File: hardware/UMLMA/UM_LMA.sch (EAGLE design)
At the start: 10 parts, among them IC1 TINY13, J1 AVRISP6_TP

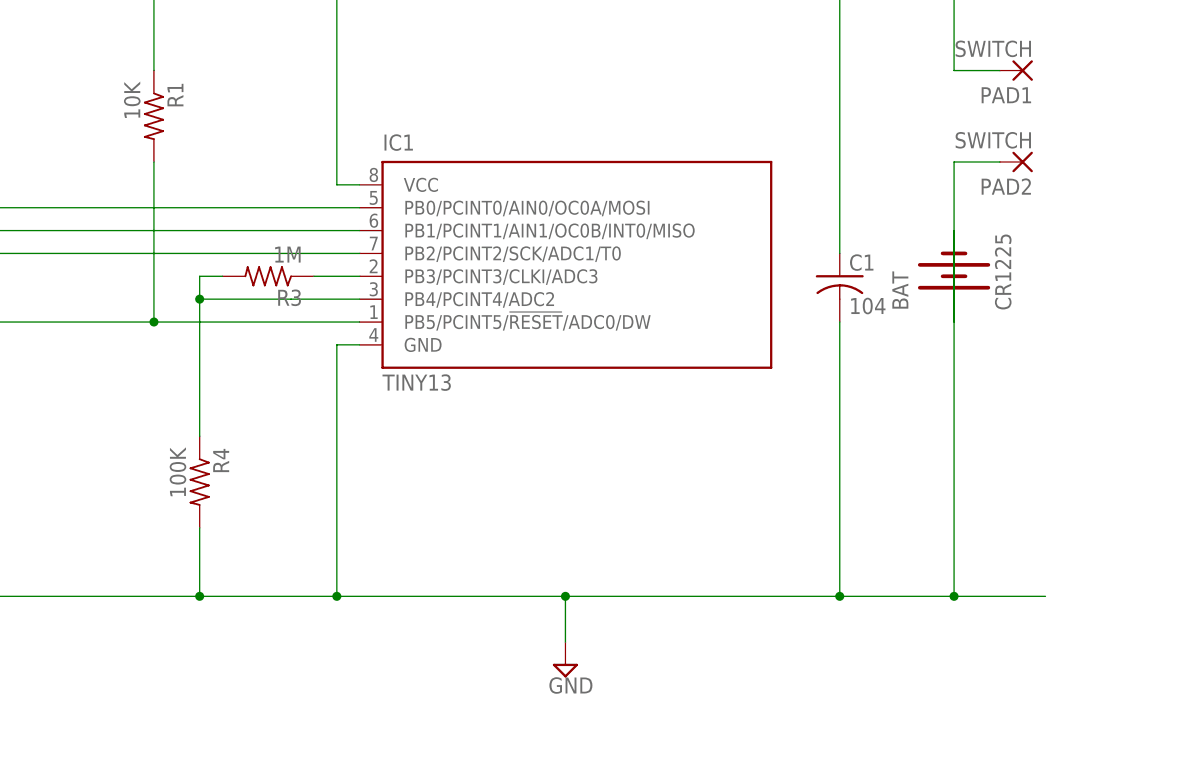
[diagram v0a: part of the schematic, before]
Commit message: Modified schematic and board to reflect hardware changes required for low voltage detection
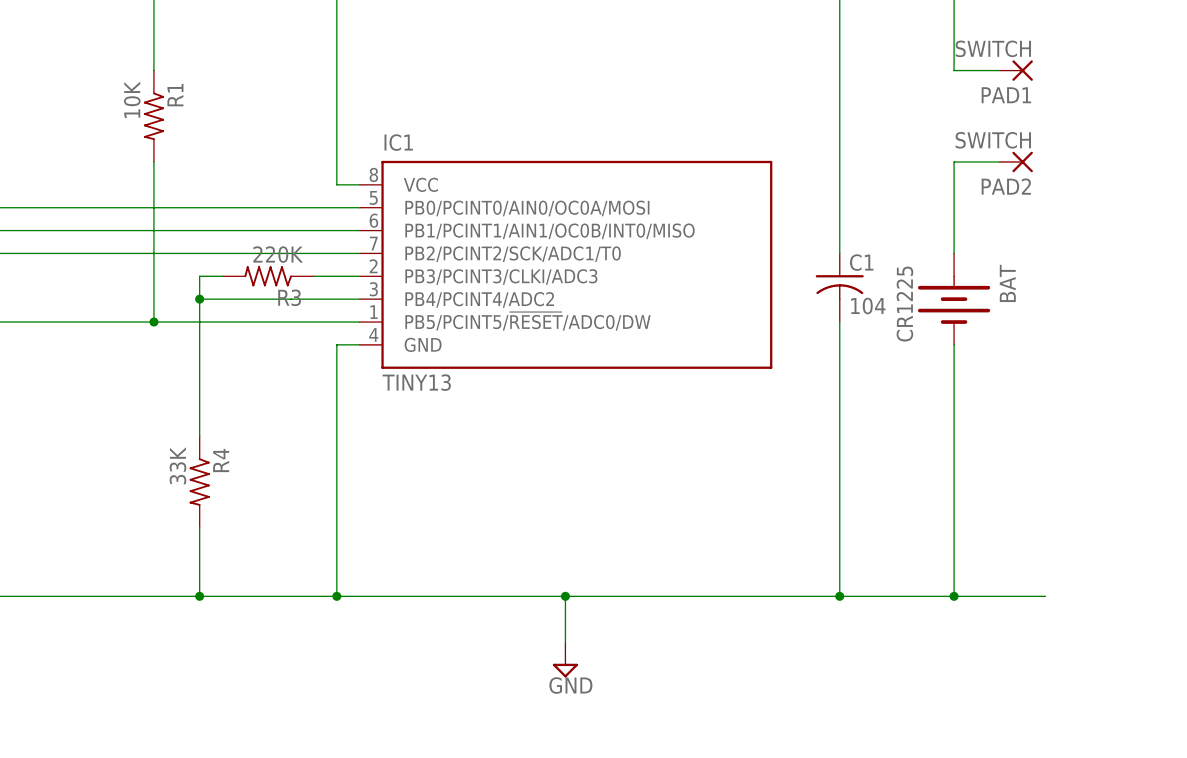
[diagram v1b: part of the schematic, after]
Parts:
- R3: value 1M -> 220K
- R4: value 100K -> 33K
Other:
- moved on the sheet: BAT
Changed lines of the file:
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@@
 <?xml version="1.0" encoding="utf-8"?>
 <!DOCTYPE eagle SYSTEM "eagle.dtd">
-<eagle version="6.4">
+<eagle version="7.1.0">
 <drawing>
 <settings>
@@
 <attribute name="BOM" value="EXCLUDE"/>
 </part>
-<part name="R3" library="rcl" deviceset="R-US_" device="R0603" value="1M">
+<part name="R3" library="rcl" deviceset="R-US_" device="R0603" value="220K">
 <attribute name="PARTNO" value="ERJ-3GEYJ102V"/>
 </part>
-<part name="R4" library="rcl" deviceset="R-US_" device="R0603" value="100K">
+<part name="R4" library="rcl" deviceset="R-US_" device="R0603" value="33K">
 <attribute name="PARTNO" value="ERJ-3GEYJ102V"/>
 </part>
@@
 <attribute name="PARTNO" x="99.06" y="71.12" size="1.778" layer="96" display="off"/>
 </instance>
-<instance part="BAT" gate="G$1" x="182.88" y="93.98" rot="R90">
-<attribute name="BOM" x="182.88" y="93.98" size="2.54" layer="96" display="off"/>
+<instance part="BAT" gate="G$1" x="182.88" y="91.44" rot="R270">
+<attribute name="BOM" x="182.88" y="91.44" size="2.54" layer="96" rot="R180" display="off"/>
 </instance>
 <instance part="FRAME1" gate="G$1" x="0" y="0"/>
@@
 <segment>
 <wire x1="182.88" y1="58.42" x2="193.04" y2="58.42" width="0.1524" layer="91"/>
-<wire x1="182.88" y1="99.06" x2="182.88" y2="58.42" width="0.1524" layer="91"/>
+<wire x1="182.88" y1="86.36" x2="182.88" y2="58.42" width="0.1524" layer="91"/>
 <wire x1="170.18" y1="58.42" x2="182.88" y2="58.42" width="0.1524" layer="91"/>
 <wire x1="170.18" y1="88.9" x2="170.18" y2="58.42" width="0.1524" layer="91"/>
@@
 <segment>
 <wire x1="187.96" y1="106.68" x2="182.88" y2="106.68" width="0.1524" layer="91"/>
-<wire x1="182.88" y1="88.9" x2="182.88" y2="106.68" width="0.1524" layer="91"/>
+<wire x1="182.88" y1="96.52" x2="182.88" y2="106.68" width="0.1524" layer="91"/>
 <pinref part="PAD2" gate="G$1" pin="P"/>
 <pinref part="BAT" gate="G$1" pin="+"/>

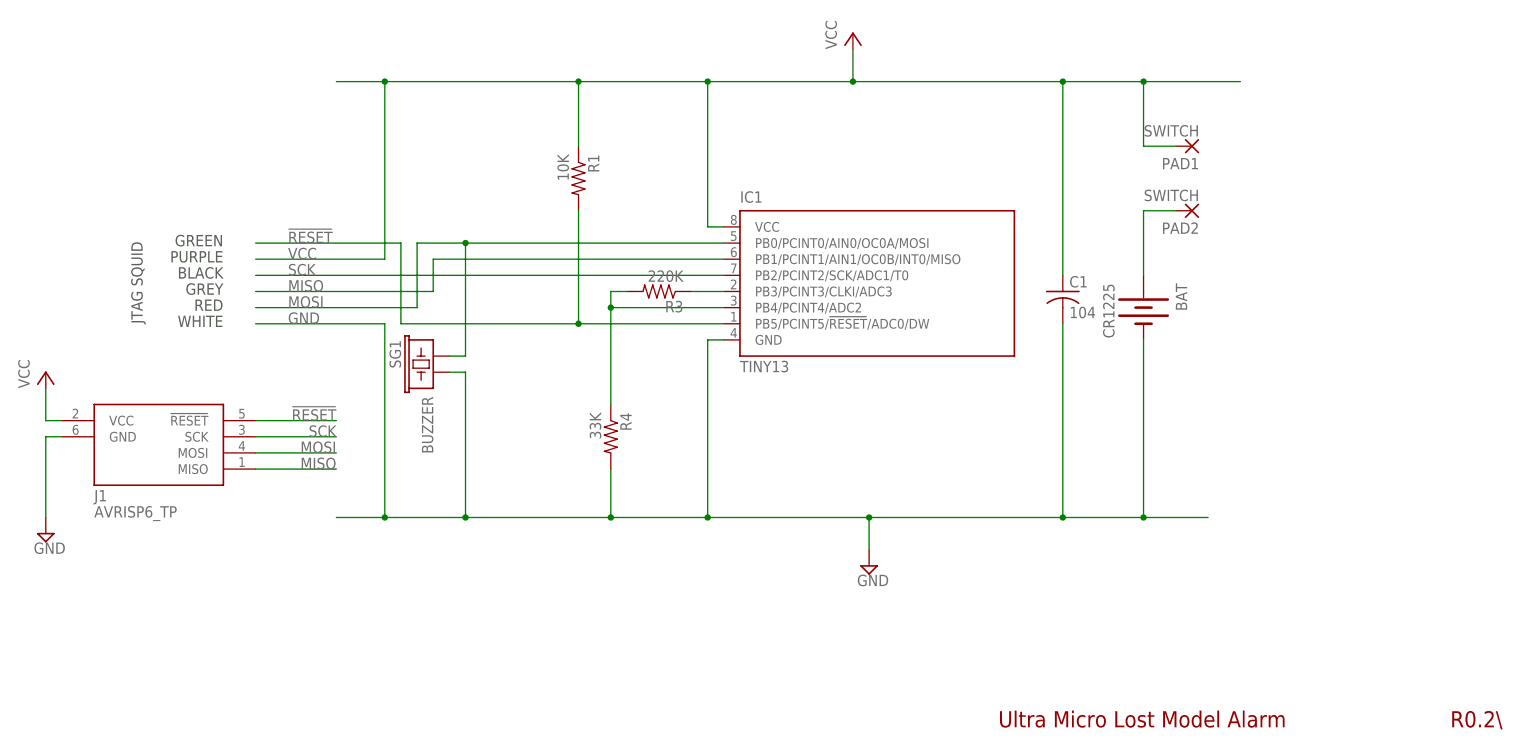
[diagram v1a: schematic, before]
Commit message: starting to convert to tiny25, config button, trying to re-do layout
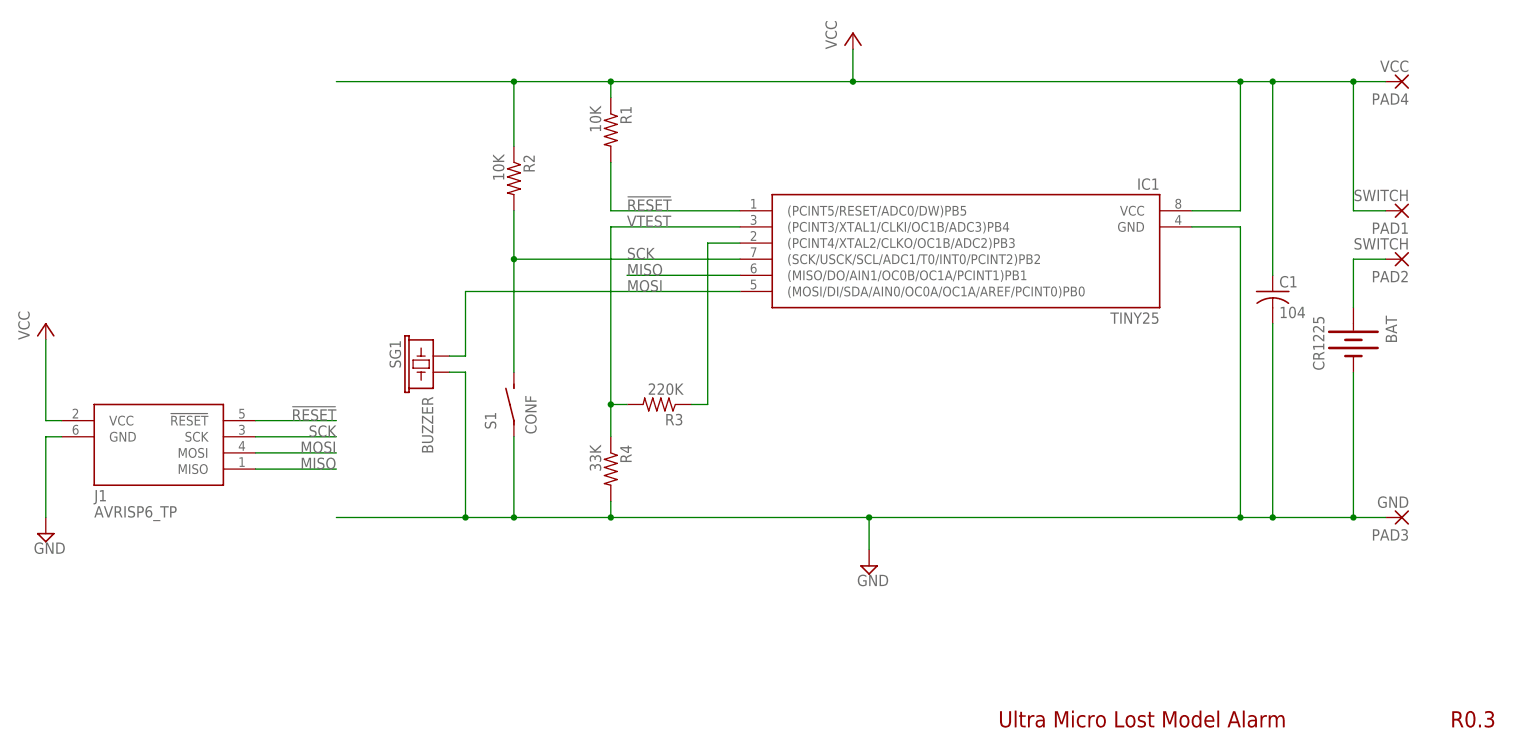
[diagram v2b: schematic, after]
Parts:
- added PAD3: GND, wirepad:WIREPAD1,6/0,8
- added PAD4: VCC, wirepad:WIREPAD1,6/0,8
- added R2: 10K, rcl:R-US_R0603
- added S1: CONF, bt_electromech:SPST_3X4X2
- IC1: value TINY13 -> TINY25; device atmel:TINY13V-10SSU -> bt_avr:TINY25-20SSU; PARTNO ATTINY13V-10SSU -> (none)
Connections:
- removed net N$3: IC1.PB4/PCINT4/ADC2, R3.2, R4.1
- new net VTEST: IC1.(PCINT3/XTAL1/CLKI/OC1B/ADC3)PB4, R3.2, R4.1
- net !RESET: now also IC1.(PCINT5/RESET/ADC0/DW)PB5; no longer IC1.PB5/PCINT5/!RESET!/ADC0/DW
- net GND: now also PAD3.P, S1.P
- net MISO: now also IC1.(MISO/DO/AIN1/OC0B/OC1A/PCINT1)PB1; no longer IC1.PB1/PCINT1/AIN1/OC0B/INT0/MISO
- net MOSI: now also IC1.(MOSI/DI/SDA/AIN0/OC0A/OC1A/AREF/PCINT0)PB0; no longer IC1.PB0/PCINT0/AIN0/OC0A/MOSI
- net N$5: now also IC1.(PCINT4/XTAL2/CLKO/OC1B/ADC2)PB3; no longer IC1.PB3/PCINT3/CLKI/ADC3
- net SCK: now also IC1.(SCK/USCK/SCL/ADC1/T0/INT0/PCINT2)PB2, R2.2, S1.S; no longer IC1.PB2/PCINT2/SCK/ADC1/T0
- net VCC: now also PAD4.P, R2.1
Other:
- note added: "R0.3"
- note removed: "BLACK"
- note removed: "GREEN"
- note removed: "GREY"
- note removed: "JTAG SQUID"
- note removed: "PURPLE"
- note removed: "R0.2\"
- note removed: "RED"
- note removed: "WHITE"
- moved on the sheet: BAT, C1, PAD1, PAD2, R1, R3, R4
